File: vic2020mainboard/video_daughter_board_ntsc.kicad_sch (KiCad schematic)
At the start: 38 parts, among them J4 Chroma Disconnect, Q1 2sc1959, Q2 2SC1815, U1 7402, U20 6560, Y1 Crystal

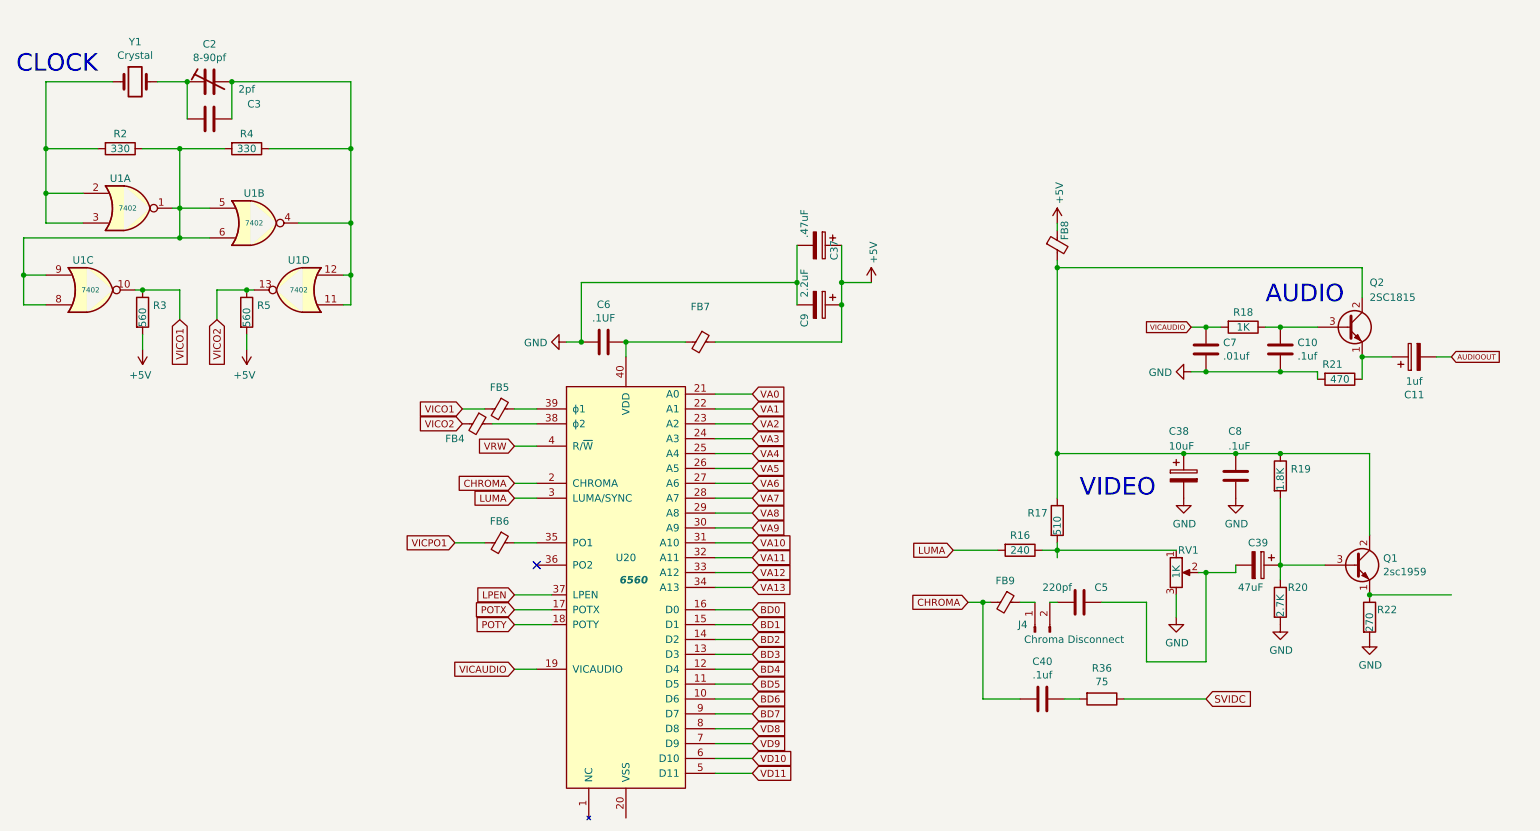
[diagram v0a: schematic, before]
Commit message: Added power supply circuit for 9V AC input
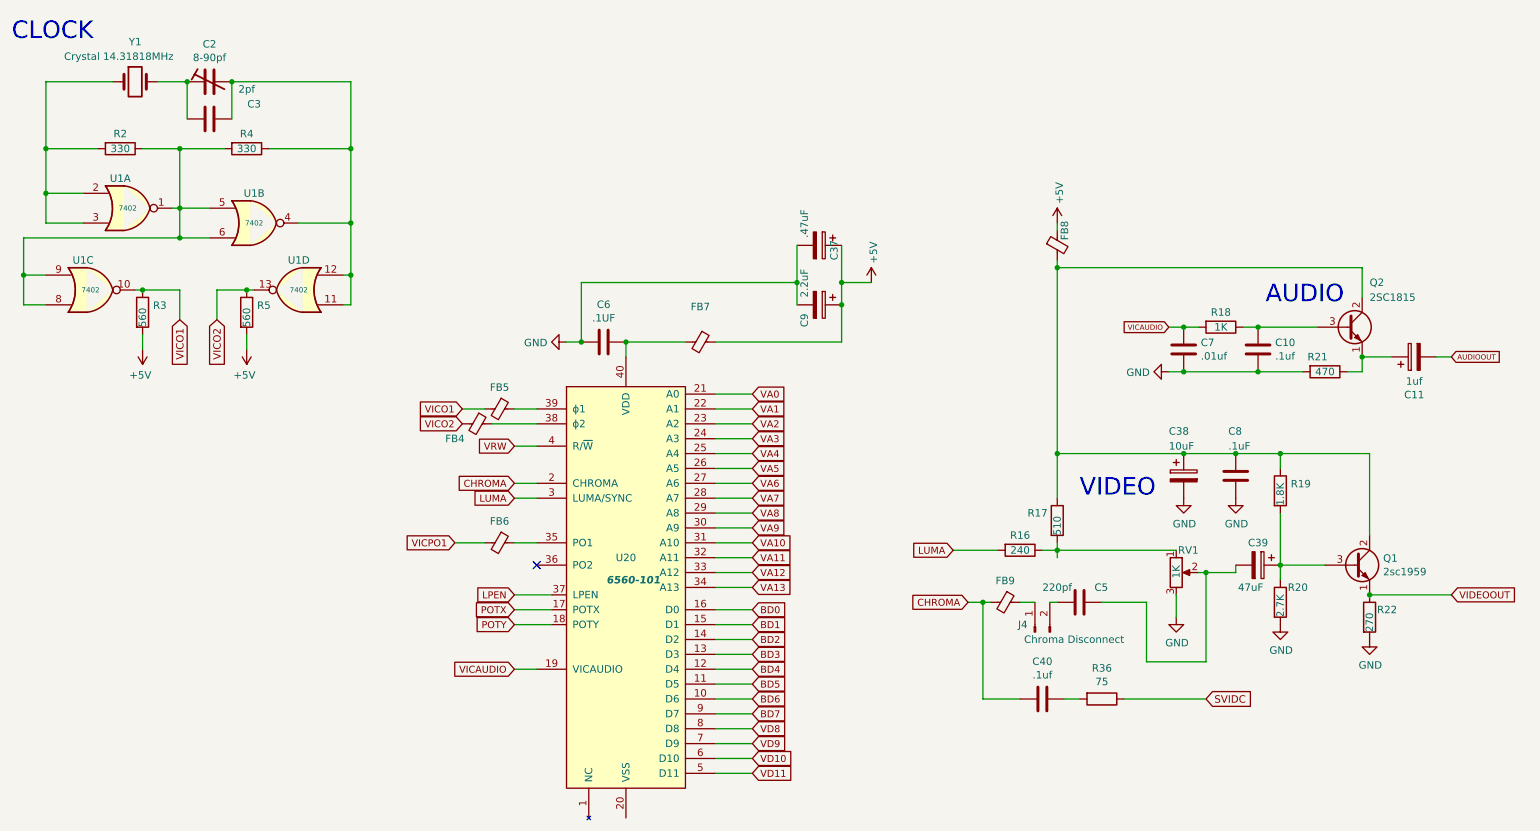
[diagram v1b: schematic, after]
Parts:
- U20: value 6560 -> 6560-101
- Y1: value Crystal -> Crystal 14.31818MHz
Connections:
- net VIDEOOUT: now reaches Q1.1 (E), R22.1
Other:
- moved on the sheet: C10, C7, R18, R19, R21
